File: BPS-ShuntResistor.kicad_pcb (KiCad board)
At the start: 2 copper layers, 37.6 x 32.5 mm, 7 parts, among them J1 Amp_Conn

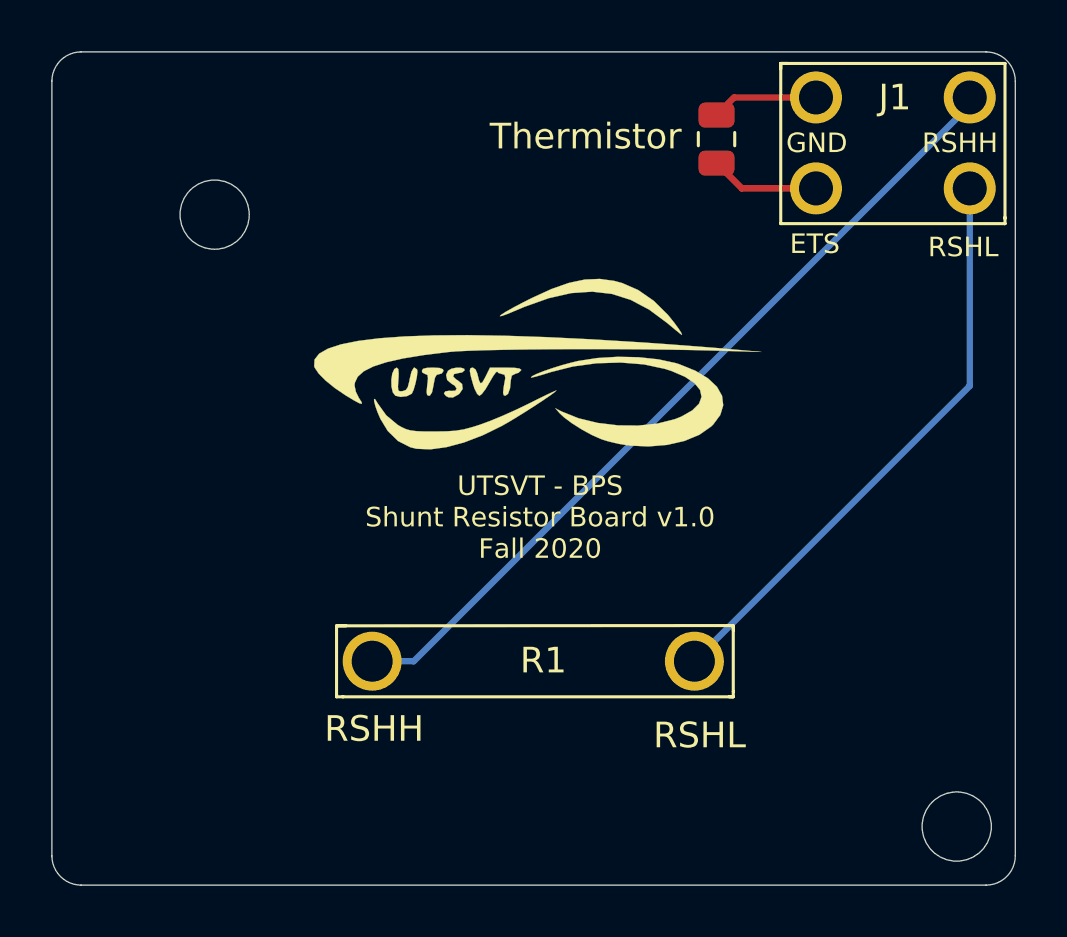
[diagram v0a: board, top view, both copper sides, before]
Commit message: banana connectors for rshh and rshl
10mm track width on top to handle up to 130A current, bottom of board is normal connectors from the 4 pin connector
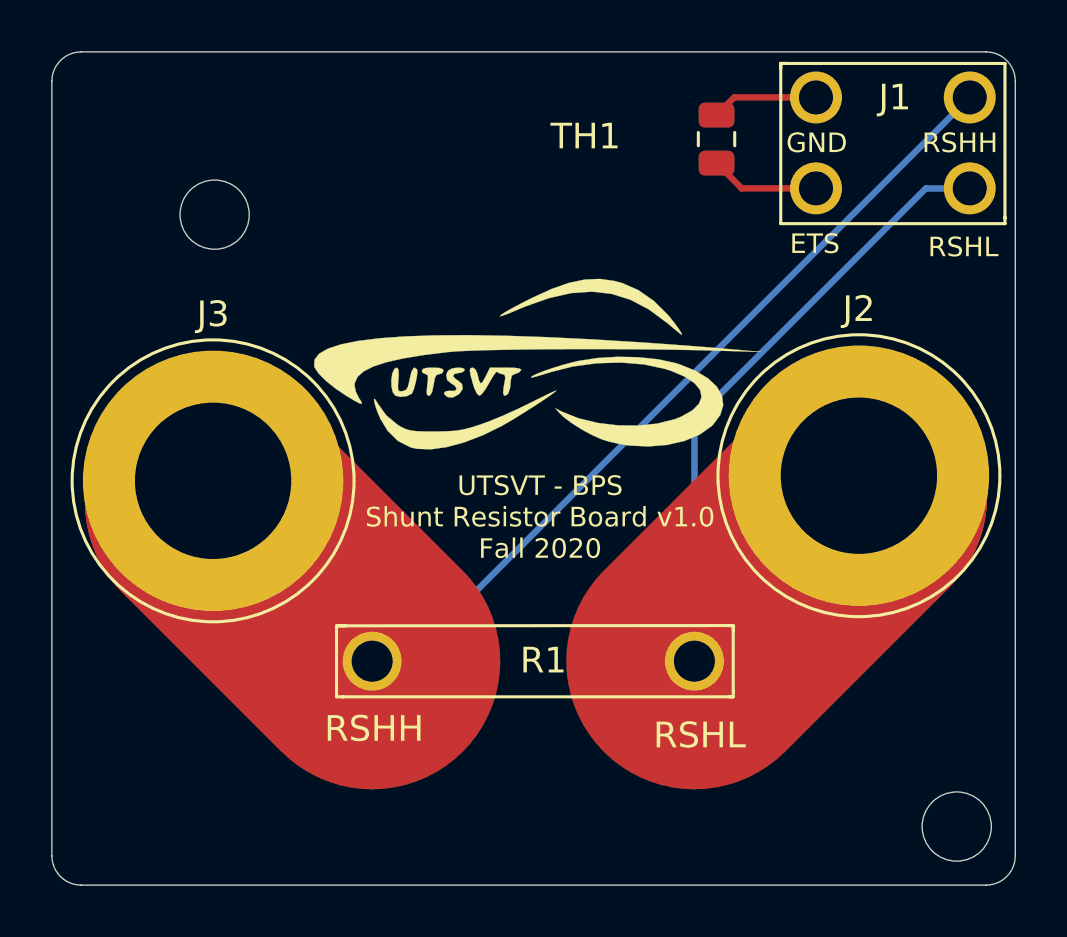
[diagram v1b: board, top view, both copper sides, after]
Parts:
- added J2: Conn_01x01_Female, Connector:Banana_Jack_1Pin, F.Cu at (175.0, 88.8)
- added J3: Conn_01x01_Female, Connector:Banana_Jack_1Pin, F.Cu at (149.8, 89.0)
- renumbered Thermistor to TH1
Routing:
- net /RSHL: track 22.9 -> 33.8 mm
- net /RSHH: track 32.6 -> 42.3 mm
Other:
- net class Default removed

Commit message: a
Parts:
- removed H1, H2: MountingHole, MountingHole:MountingHole_2.7mm_M2.5
- removed J1: Amp_Conn, UTSVT_Connectors:Power_Metal_Strip_Battery_Shunt_Resistor_4_Pin_Connector
- removed J2, J3: Conn_01x01_Female, Connector:Banana_Jack_1Pin
- removed R1: 100u, UTSVT_Passive:Power_Metal_Strip_Battery_Shunt_Resistor
- removed TH1: 100, Resistor_SMD:R_0805_2012Metric
- moved LOGO1 33.7 mm to (194.6, 94.0)
- moved LOGO2 33.7 mm to (195.7, 94.1)
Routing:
- net /RSHH: track 42.3 -> 0.00 mm
- net /RSHL: track 33.8 -> 0.00 mm
- net /ETS: track 4.29 -> 0.00 mm
- net /GND: track 4.17 -> 0.00 mm
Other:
- board size 37.6 x 32.5 mm -> 103.1 x 76.2 mm
- board text removed: "ETS"
- board text removed: "GND"
- board text removed: "RSHH"
- board text removed: "RSHL"

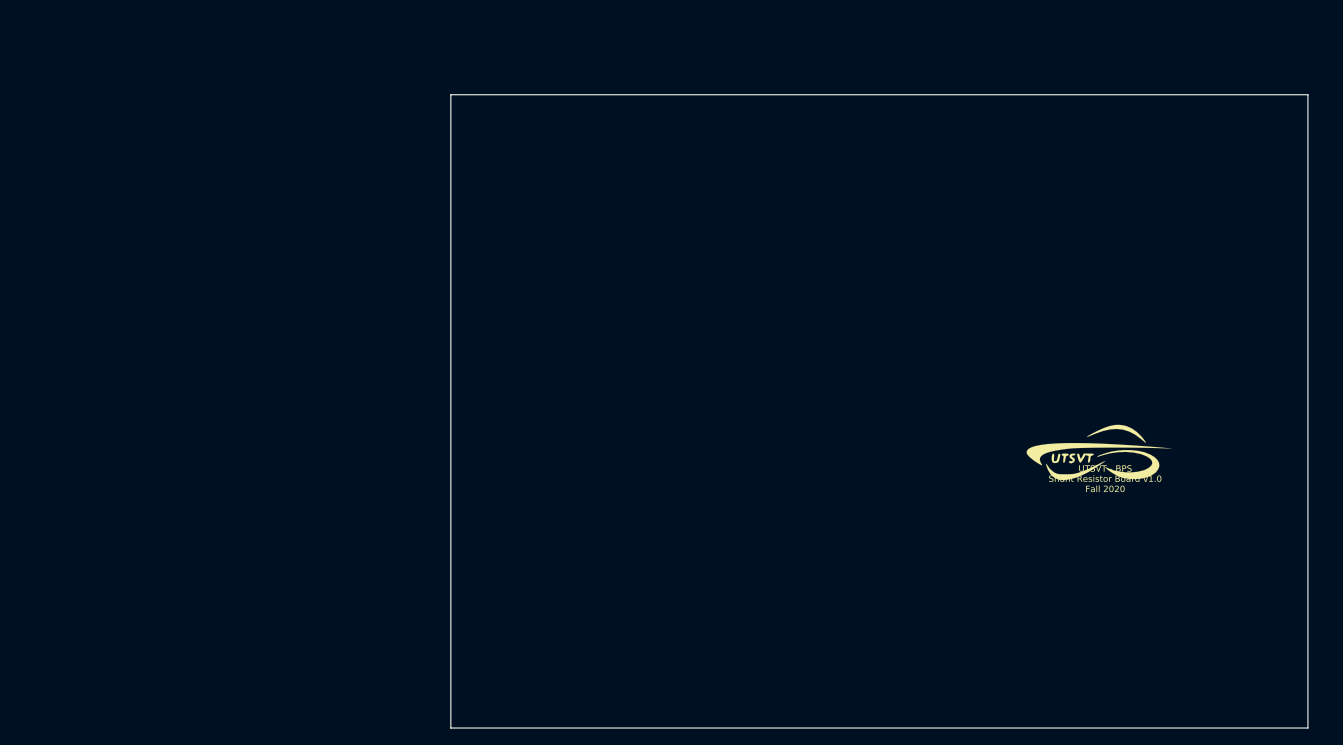
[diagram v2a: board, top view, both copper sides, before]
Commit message: working on new board
connector for current board, testing for shunt
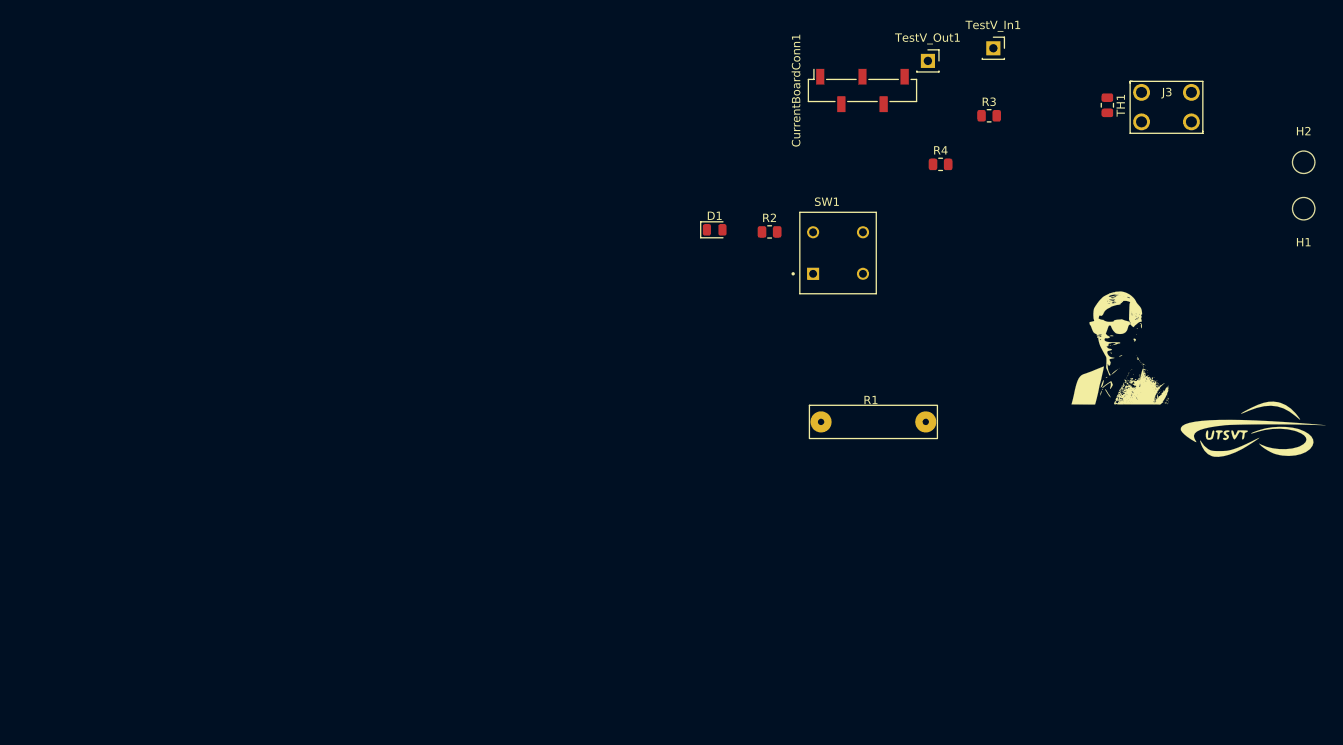
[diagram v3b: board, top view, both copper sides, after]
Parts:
- added CurrentBoardConn1: Conn_01x05_Female, Connector_PinSocket_2.54mm:PinSocket_1x05_P2.54mm_Vertical_SMD_Pin1Right, F.Cu at (166.4, 50.3)
- added D1: LED, LED_SMD:LED_0805_2012Metric, F.Cu at (148.6, 67.1)
- added H1: MountingHole, MountingHole:MountingHole_2.7mm_M2.5, F.Cu at (219.5, 64.5)
- added H2: MountingHole, MountingHole:MountingHole_2.7mm_M2.5, F.Cu at (219.5, 58.9)
- added J3: Amp_Conn, UTSVT_Connectors:Power_Metal_Strip_Battery_Shunt_Resistor_4_Pin_Connector, F.Cu at (202.9, 52.1)
- added R1: 100u, UTSVT_Passive:Vishay_100u_Shunt, F.Cu at (167.4, 90.2)
- added R2: 1.6k, Resistor_SMD:R_0805_2012Metric, F.Cu at (155.2, 67.3)
- added R3: 34k, Resistor_SMD:R_0805_2012Metric, F.Cu at (181.6, 53.3)
- added R4: 51, Resistor_SMD:R_0805_2012Metric, F.Cu at (175.8, 59.2)
- added SW1: SW_DPST, UTSVT_Passive:SW_PVA1EEH1, F.Cu at (163.4, 69.8)
- added TH1: 100, Resistor_SMD:R_0805_2012Metric, F.Cu at (195.8, 52.1)
- added TestV_In1: TestV_In, Connector_PinSocket_2.54mm:PinSocket_1x01_P2.54mm_Vertical, F.Cu at (182.1, 45.2)
- added TestV_Out1: TestV_Out, Connector_PinSocket_2.54mm:PinSocket_1x01_P2.54mm_Vertical, F.Cu at (174.2, 46.7)
- LOGO2: moved to F.Cu
- moved LOGO1 18.8 mm to (213.1, 91.2)
- moved LOGO2 13.1 mm to (196.9, 81.1), turned to 0 degrees
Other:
- board outline removed
- board text removed: "Dr. Gary Hallock"
- board text removed: "UTSVT - BPS Shunt Resistor Board v1.0 Fall 2020"

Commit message: pcb v1 not done
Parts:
- TestV_In1, TestV_Out1: footprint Connector_PinSocket_2.54mm:PinSocket_1x01_P2.54mm_Vertical -> Connector_PinHeader_2.54mm:PinHeader_1x01_P2.54mm_Vertical
- moved TestV_In1 114.7 mm to (68.0, 56.2)
- moved TestV_Out1 107.1 mm to (68.1, 60.7)
- moved J3 102.8 mm to (100.3, 57.9)
- moved TH1 101.3 mm to (94.7, 57.9)
- moved R3 92.3 mm to (89.4, 57.9), turned to -90 degrees
- moved R4 86.4 mm to (89.4, 62.7), turned to -90 degrees
- moved CurrentBoardConn1 85.0 mm to (84.3, 72.4)
- moved SW1 82.4 mm to (81.6, 59.9)
- moved R1 81.8 mm to (85.9, 83.6)
- moved R2 81.4 mm to (74.4, 57.1)
- moved D1 73.8 mm to (74.9, 63.2), turned to 90 degrees
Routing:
- net RSHL: track 0.00 -> 71.5 mm, vias 0 -> 2
- net GND: track 0.00 -> 34.4 mm, vias 0 -> 3
- net RSHH: track 0.00 -> 32.9 mm
- net Net-(R1-Pad1): track 0.00 -> 24.1 mm
- net Net-(R3-Pad1): track 0.00 -> 22.3 mm, vias 0 -> 1
- net Net-(D1-Pad2): track 0.00 -> 5.75 mm
- net Net-(R2-Pad2): track 0.00 -> 3.43 mm
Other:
- board outline added: 40.1 x 35.1 mm

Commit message: added more info per manthan
might need more changes
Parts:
- CurrentBoardConn1: footprint Connector_PinSocket_2.54mm:PinSocket_1x05_P2.54mm_Vertical_SMD_Pin1Right -> Connector_PinSocket_2.54mm:PinSocket_1x05_P2.54mm_Vertical
- LOGO1, LOGO2: moved to B.Cu
- TestV_In1: value TestV_In -> 0-5V
- TestV_Out1: value TestV_Out -> 0-5V
- moved H2 150.7 mm to (69.1, 69.5)
- moved H1 150.6 mm to (69.2, 75.3)
- moved LOGO1 127.6 mm to (86.2, 78.2), turned to 180 degrees
- moved LOGO2 98.4 mm to (98.5, 81.2), turned to 180 degrees
- moved CurrentBoardConn1 3.33 mm to (81.0, 73.0)
- renumbered SW1 to LED_BATT_Switch1
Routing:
- net ETS: track 0.00 -> 36.2 mm, vias 0 -> 2
- net +3V3: track 0.00 -> 27.9 mm, vias 0 -> 2
- net RSHH: track 32.9 -> 39.6 mm, vias 0 -> 2
- net GND: track 34.4 -> 36.3 mm
- net RSHL: track 71.5 -> 70.3 mm

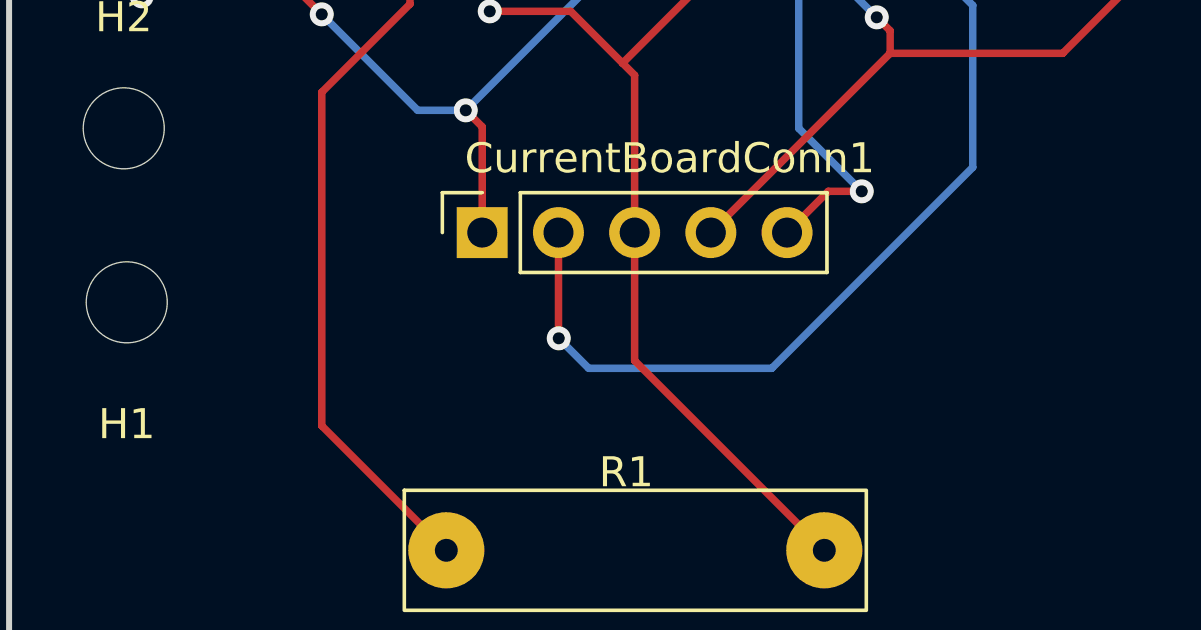
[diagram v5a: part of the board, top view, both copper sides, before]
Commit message: Adjusting shunt-current connector pins
Tianda and I haven't really decided on footprint stuff yet but pins now line up.
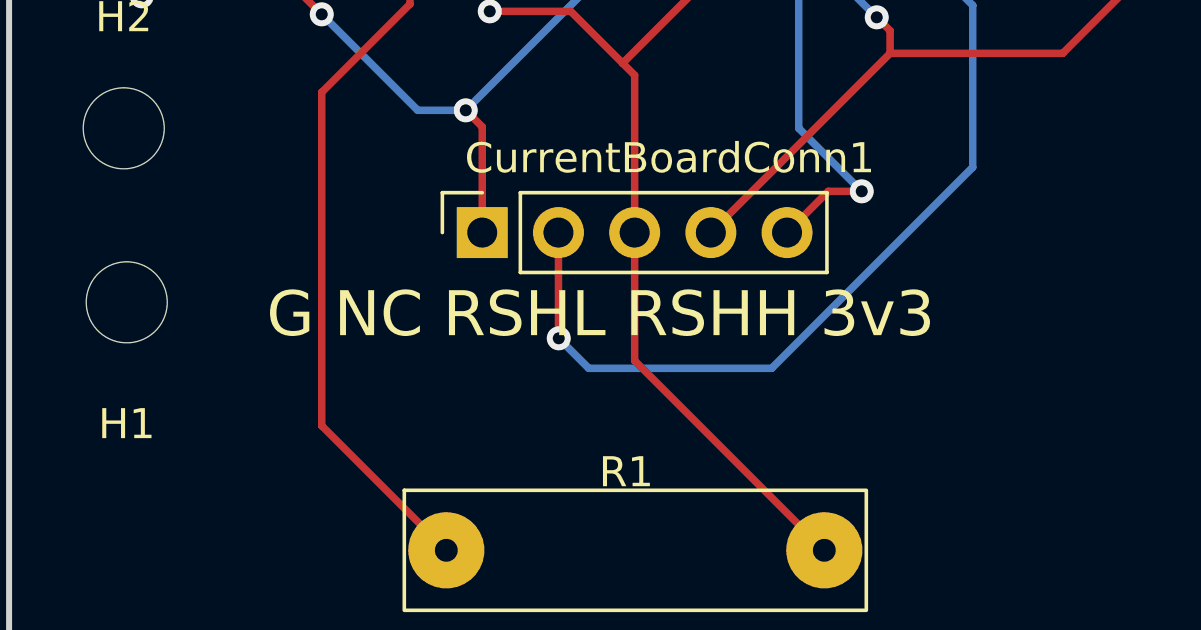
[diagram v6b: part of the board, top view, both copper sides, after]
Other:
- board text added: "G NC RSHL RSHH 3v3"
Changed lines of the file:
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@@
   )
   (gr_rect (start 65.278 54.356) (end 105.378 89.456) (layer "Edge.Cuts") (width 0.2) (fill none))
+  (gr_text "G NC RSHL RSHH 3v3" (at 85 75.7) (layer "F.SilkS")
+    (effects (font (size 1.5 1.5) (thickness 0.3)))
+  )
   (dimension (type aligned) (layer "Cmts.User")
     (pts (xy 105.378 54.356) (xy 105.378 89.456))
